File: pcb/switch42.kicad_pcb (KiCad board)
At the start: 2 copper layers, 114.3 x 81 mm, 83 parts, among them J1 MJ-4PP-9, SW1 SW_PUSH, SW10 SW_PUSH, SW11 SW_PUSH, SW12 SW_PUSH, SW13 SW_PUSH, SW14 SW_PUSH, SW15 SW_PUSH, SW16 SW_PUSH, SW17 SW_PUSH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

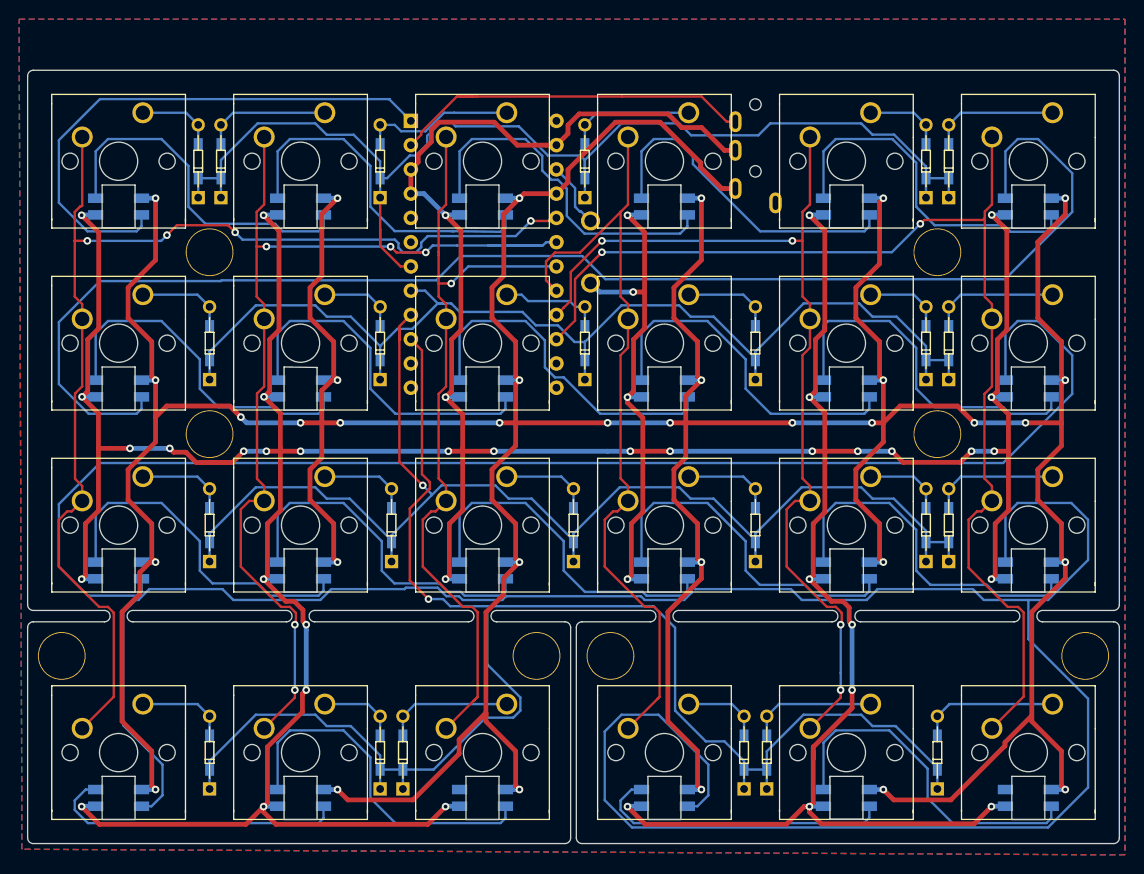
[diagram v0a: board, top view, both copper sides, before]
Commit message: Slightly modify footprint silks
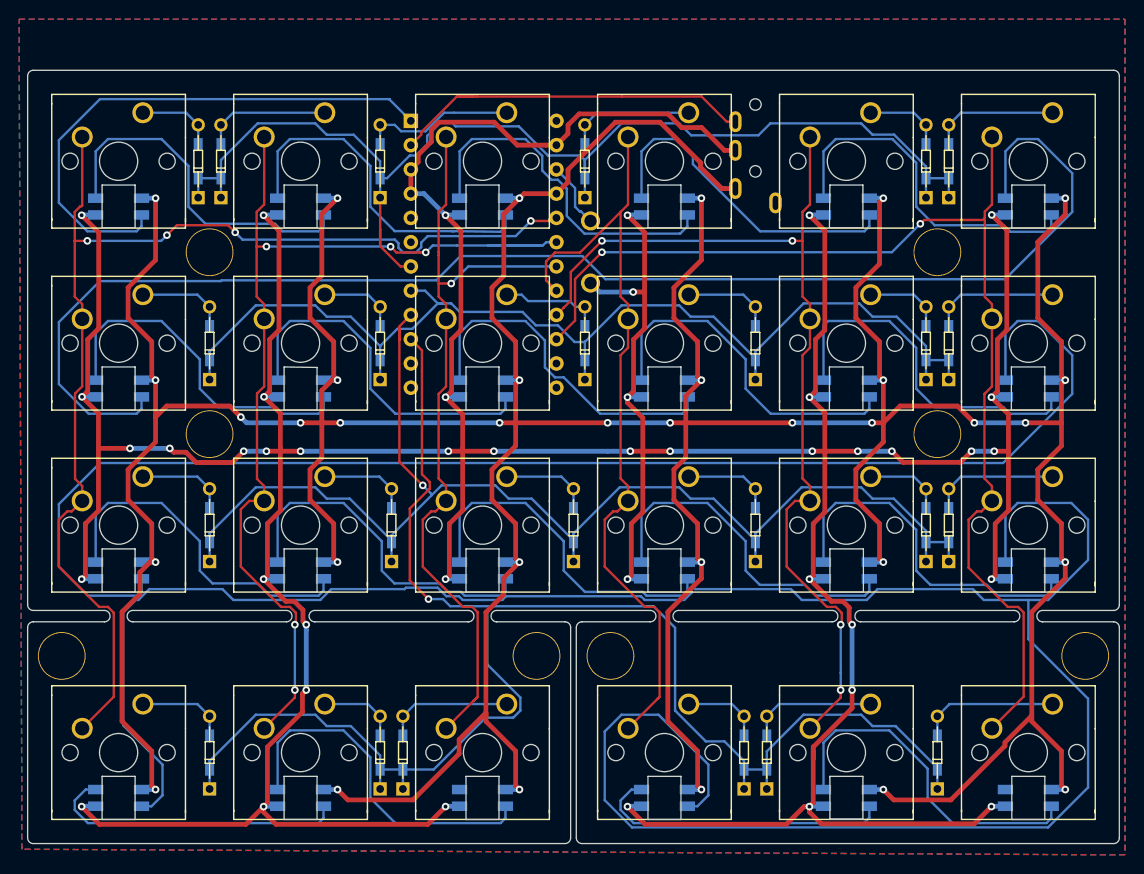
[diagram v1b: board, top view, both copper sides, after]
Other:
- board text added: "* switch42 v0.21 designed by @zk_phi *"
- board text removed: "* switch42 v0.2 designed by @zk_phi *"

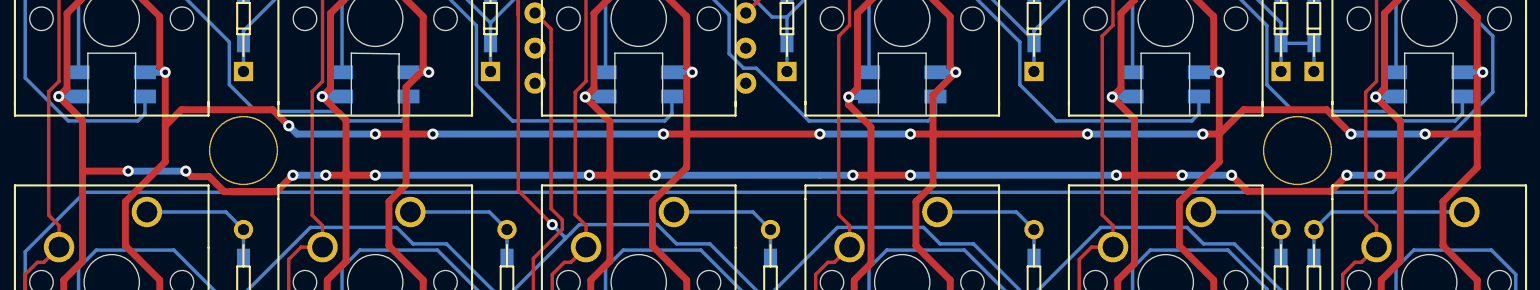
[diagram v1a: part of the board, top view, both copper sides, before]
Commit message: Refactoring: Reduce redundant vias
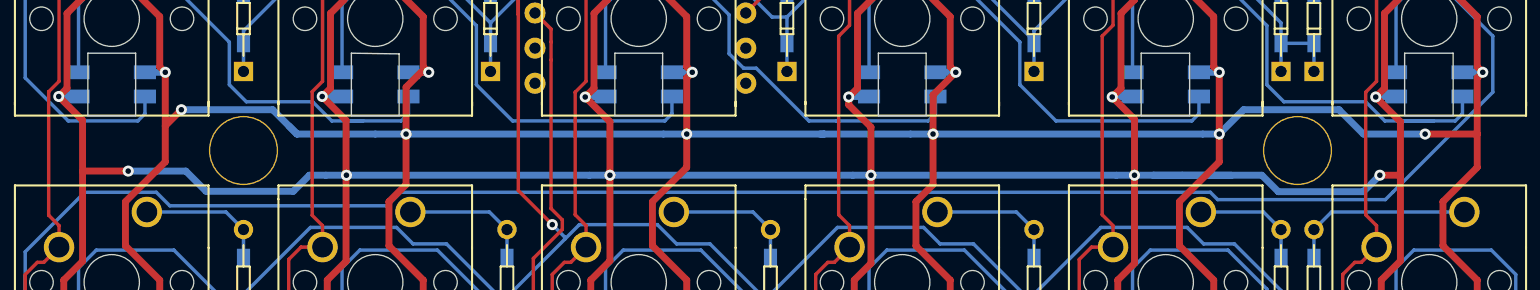
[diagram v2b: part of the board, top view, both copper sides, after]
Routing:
- net GND: track 576.0 -> 578.7 mm, vias 43 -> 35
- net Net-(L18-Pad1): track 37.8 -> 40.0 mm
- net VCC: track 568.5 -> 569.6 mm, vias 34 -> 30
- net Net-(L22-Pad1): track 146.8 -> 147.9 mm
- net Net-(L2-Pad1): track 36.6 -> 37.6 mm

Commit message: Add pads for LED strip and uniform the weight of silk text
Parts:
- added J2: Conn_01x03, kbd:StripLED_rev-irreversible, F.Cu at (74.2, 75.9)
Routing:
- net led: track 57.2 -> 103.5 mm, vias 0 -> 2
- net GND: track 578.7 -> 582.8 mm
- net VCC: track 569.6 -> 571.0 mm
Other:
- board text added: "GND"
- board text added: "LED"
- board text added: "Vcc"

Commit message: Change silk texts for the LED strip
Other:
- board text added: "+"
- board text added: "-"
- board text removed: "GND"
- board text removed: "LED"
- board text removed: "Vcc"
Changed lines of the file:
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@@
   (general
     (thickness 1.6)
-    (drawings 171)
+    (drawings 172)
     (tracks 1252)
     (zones 0)
@@
       (net 32 GND))
   )
-  (gr_text GND (at 76.830332 75.83109) (layer B.SilkS)
+  (gr_line (start 74.15141 77.021722) (end 75.6397 77.021722) (layer B.SilkS) (width 0.12))
+  (gr_line (start 74.15141 69.580272) (end 75.6397 69.580272) (layer B.SilkS) (width 0.12))
+  (gr_text - (at 75.6397 75.83109) (layer B.SilkS)
     (effects (font (size 1 1) (thickness 0.15)) (justify mirror))
   )
-  (gr_text LED (at 76.532674 73.449826) (layer B.SilkS)
+  (gr_text + (at 75.6397 70.770904) (layer B.SilkS)
     (effects (font (size 1 1) (thickness 0.15)) (justify mirror))
   )
-  (gr_text Vcc (at 76.532674 70.770904) (layer B.SilkS)
-    (effects (font (size 1 1) (thickness 0.15)) (justify mirror))
-  )

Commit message: Make diode line around thumb clusters safer
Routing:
- net row3: track 168.3 -> 175.1 mm, vias 1 -> 3
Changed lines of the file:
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@@
     (thickness 1.6)
     (drawings 172)
-    (tracks 1252)
+    (tracks 1255)
     (zones 0)
     (modules 84)
@@
   (segment (start 70.2818 107.978098) (end 70.2818 108.264528) (width 0.25) (layer B.Cu) (net 7) (status 30))
   (segment (start 75.121801 102.524527) (end 81.352797 102.524527) (width 0.25) (layer B.Cu) (net 7))
-  (via (at 93.201522 90.416332) (size 0.8) (drill 0.4) (layers F.Cu B.Cu) (net 7))
-  (segment (start 91.2368 88.45161) (end 93.201522 90.416332) (width 0.25) (layer F.Cu) (net 7))
-  (segment (start 91.2368 80.95242) (end 91.2368 88.45161) (width 0.25) (layer F.Cu) (net 7))
-  (segment (start 93.331207 78.162011) (end 93.331207 78.858013) (width 0.25) (layer F.Cu) (net 7))
-  (segment (start 92.517615 77.348419) (end 93.331207 78.162011) (width 0.25) (layer F.Cu) (net 7))
-  (segment (start 93.331207 78.858013) (end 91.2368 80.95242) (width 0.25) (layer F.Cu) (net 7))
-  (segment (start 95.472923 91.164001) (end 100.001248 91.164001) (width 0.25) (layer B.Cu) (net 7))
-  (segment (start 94.725254 90.416332) (end 95.472923 91.164001) (width 0.25) (layer B.Cu) (net 7))
-  (segment (start 93.201522 90.416332) (end 94.725254 90.416332) (width 0.25) (layer B.Cu) (net 7))
-  (segment (start 93.740802 108.264528) (end 90.522425 108.264528) (width 0.25) (layer B.Cu) (net 7) (status 20))
+  (via (at 92.308548 73.152168) (size 0.8) (drill 0.4) (layers F.Cu B.Cu) (net 7))
+  (segment (start 92.443133 73.017583) (end 92.308548 73.152168) (width 0.25) (layer F.Cu) (net 7))
+  (segment (start 92.443133 64.297235) (end 92.443133 73.017583) (width 0.25) (layer F.Cu) (net 7))
+  (segment (start 91.356132 63.210234) (end 92.443133 64.297235) (width 0.25) (layer F.Cu) (net 7))
+  (via (at 106.89379 74.045142) (size 0.8) (drill 0.4) (layers F.Cu B.Cu) (net 7))
+  (segment (start 93.201522 74.045142) (end 106.89379 74.045142) (width 0.25) (layer B.Cu) (net 7))
+  (segment (start 92.308548 73.152168) (end 93.201522 74.045142) (width 0.25) (layer B.Cu) (net 7))
+  (via (at 106.89379 90.956964) (size 0.8) (drill 0.4) (layers F.Cu B.Cu) (net 7))
+  (segment (start 106.89379 74.045142) (end 106.89379 90.956964) (width 0.25) (layer F.Cu) (net 7))
+  (segment (start 126.241175 107.364528) (end 126.241175 108.264528) (width 0.25) (layer B.Cu) (net 7))
+  (segment (start 124.191174 105.314527) (end 126.241175 107.364528) (width 0.25) (layer B.Cu) (net 7))
+  (segment (start 122.242797 105.314527) (end 124.191174 105.314527) (width 0.25) (layer B.Cu) (net 7))
+  (segment (start 119.021799 102.093529) (end 122.242797 105.314527) (width 0.25) (layer B.Cu) (net 7))
   (segment (start 99.170801 102.834529) (end 93.740802 108.264528) (width 0.25) (layer B.Cu) (net 7))
-  (segment (start 102.821801 102.093529) (end 102.080801 102.834529) (width 0.25) (layer B.Cu) (net 7))
+  (segment (start 93.740802 108.264528) (end 90.522425 108.264528) (width 0.25) (layer B.Cu) (net 7))
+  (segment (start 102.080801 102.834529) (end 99.170801 102.834529) (width 0.25) (layer B.Cu) (net 7))
   (segment (start 102.821801 100.725527) (end 102.821801 102.093529) (width 0.25) (layer B.Cu) (net 7))
   (segment (start 99.347564 97.25129) (end 102.821801 100.725527) (width 0.25) (layer B.Cu) (net 7))
+  (segment (start 102.821801 102.093529) (end 102.080801 102.834529) (width 0.25) (layer B.Cu) (net 7))
   (segment (start 99.347564 91.817685) (end 99.347564 97.25129) (width 0.25) (layer B.Cu) (net 7))
-  (segment (start 102.080801 102.834529) (end 99.170801 102.834529) (width 0.25) (layer B.Cu) (net 7))
-  (segment (start 100.001248 91.164001) (end 99.347564 91.817685) (width 0.25) (layer B.Cu) (net 7))
-  (segment (start 126.241175 107.364528) (end 126.241175 108.264528) (width 0.25) (layer B.Cu) (net 7) (status 20))
-  (segment (start 124.191174 105.314527) (end 126.241175 107.364528) (width 0.25) (layer B.Cu) (net 7))
-  (segment (start 122.242797 105.314527) (end 124.191174 105.314527) (width 0.25) (layer B.Cu) (net 7))
-  (segment (start 100.001248 91.164001) (end 116.762912 91.164001) (width 0.25) (layer B.Cu) (net 7))
-  (segment (start 119.021799 102.093529) (end 122.242797 105.314527) (width 0.25) (layer B.Cu) (net 7))
-  (segment (start 119.021799 93.422888) (end 119.021799 102.093529) (width 0.25) (layer B.Cu) (net 7))
-  (segment (start 116.762912 91.164001) (end 119.021799 93.422888) (width 0.25) (layer B.Cu) (net 7))
-  (segment (start 92.517615 65.302955) (end 92.517615 66.603692) (width 0.25) (layer F.Cu) (net 7))
-  (segment (start 91.356132 63.210234) (end 92.517615 64.371717) (width 0.25) (layer F.Cu) (net 7))
-  (segment (start 92.517615 66.603692) (end 92.517615 77.348419) (width 0.25) (layer F.Cu) (net 7))
-  (segment (start 92.517615 64.371717) (end 92.517615 65.302955) (width 0.25) (layer F.Cu) (net 7))
+  (segment (start 99.933295 91.231954) (end 99.347564 91.817685) (width 0.25) (layer B.Cu) (net 7))
+  (segment (start 106.053115 91.231954) (end 99.933295 91.231954) (width 0.25) (layer B.Cu) (net 7))
+  (segment (start 106.328105 90.956964) (end 106.053115 91.231954) (width 0.25) (layer B.Cu) (net 7))
+  (segment (start 106.89379 90.956964) (end 106.328105 90.956964) (width 0.25) (layer B.Cu) (net 7))
+  (segment (start 116.79208 91.231954) (end 119.021799 93.461673) (width 0.25) (layer B.Cu) (net 7))
+  (segment (start 107.734465 91.231954) (end 116.79208 91.231954) (width 0.25) (layer B.Cu) (net 7))
+  (segment (start 107.459475 90.956964) (end 107.734465 91.231954) (width 0.25) (layer B.Cu) (net 7))
+  (segment (start 119.021799 93.461673) (end 119.021799 94.583544) (width 0.25) (layer B.Cu) (net 7))
+  (segment (start 106.89379 90.956964) (end 107.459475 90.956964) (width 0.25) (layer B.Cu) (net 7))
+  (segment (start 119.021799 94.583544) (end 119.021799 102.093529) (width 0.25) (layer B.Cu) (net 7))
+  (segment (start 119.021799 93.422888) (end 119.021799 94.583544) (width 0.25) (layer B.Cu) (net 7))
   (segment (start 70.2818 102.679528) (end 70.2818 104.714528) (width 0.25) (layer B.Cu) (net 8) (status 30))
   (segment (start 69.0118 101.409528) (end 70.2818 102.679528) (width 0.25) (layer B.Cu) (net 8) (status 20))
@@
   (segment (start 114.0968 80.137) (end 112.996801 81.236999) (width 0.25) (layer F.Cu) (net 38) (status 10))
   (segment (start 112.996801 81.236999) (end 112.527799 81.236999) (width 0.25) (layer F.Cu) (net 38))
-  (segment (start 116.830865 91.231954) (end 117.416596 91.817685) (width 0.25) (layer F.Cu) (net 38))
   (segment (start 115.863808 91.231954) (end 116.830865 91.231954) (width 0.25) (layer F.Cu) (net 38))
   (segment (start 111.651799 87.019945) (end 115.863808 91.231954) (width 0.25) (layer F.Cu) (net 38))
@@
   (segment (start 106.596132 58.130234) (end 105.509131 57.043233) (width 0.25) (layer F.Cu) (net 38))
   (segment (start 113.312581 49.884501) (end 111.47629 51.720792) (width 0.25) (layer F.Cu) (net 38))
+  (segment (start 116.830865 91.231954) (end 117.416596 91.817685) (width 0.25) (layer F.Cu) (net 38))
   (segment (start 133.1468 59.531366) (end 133.1468 61.087) (width 0.25) (layer F.Cu) (net 39) (status 20))
   (segment (start 132.362693 58.747259) (end 133.1468 59.531366) (width 0.25) (layer F.Cu) (net 39))

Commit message: Change version name
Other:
- board text added: "* switch42 v0.3 designed by @zk_phi *"
- board text removed: "* switch42 v0.21 designed by @zk_phi *"
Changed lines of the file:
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@@
     (effects (font (size 5 5) (thickness 0.15)) (justify mirror))
   )
-  (gr_text "* switch42 v0.21 designed by @zk_phi *" (at 136.957248 95.17886) (layer F.Mask)
+  (gr_text "* switch42 v0.3 designed by @zk_phi *" (at 136.957248 95.17886) (layer F.Mask)
     (effects (font (size 1.2 1.2) (thickness 0.3)))
   )
-  (gr_text "* switch42 v0.21 designed by @zk_phi *" (at 79.806912 95.17886) (layer F.Mask)
+  (gr_text "* switch42 v0.3 designed by @zk_phi *" (at 79.806912 95.17886) (layer F.Mask)
     (effects (font (size 1.2 1.2) (thickness 0.3)))
   )

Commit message: Use components from my own library
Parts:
- D1, D10, D11, D12, D13, D14, D15, D16, D17, D18, D19, D2, D20, D21, D22, D23, D24, D3, D4, D5, D6, D7, D8, D9: footprint kbd:D3_TH_SMD_irreversible -> phi-kbd-library:D_TH_SMD-irreversible
- J1: footprint SMKJP:CON_MJ-4PP-9-kbd -> phi-kbd-library:MJ-4PP-9-irreversible
- J2: footprint kbd:StripLED_rev-irreversible -> phi-kbd-library:StripLED-irreversible; moved to B.Cu
- L1, L10, L11, L12, L13, L14, L15, L16, L17, L18, L19, L2, L20, L21, L22, L23, L24, L3, L4, L5, L6, L7, L8, L9: footprint kbd:SK6812MINI_rev_irreversible -> phi-kbd-library:SK6812MINI-irreversible; moved to B.Cu
- SW1: footprint kbd:ResetSW-irreversible -> phi-kbd-library:ResetSW-irreversible; moved to B.Cu
- SW10, SW11, SW12, SW13, SW14, SW15, SW16, SW17, SW18, SW19, SW2, SW20, SW21, SW22, SW23, SW24, SW25, SW3, SW4, SW5, SW6, SW7, SW8, SW9: footprint SMKJP:SW_Cherry_MX1A_1.00u_PCB_nosilk -> phi-kbd-library:MX_1.00u-irreversible
- U1: footprint SMKJP:BOARD_Pro_Micro_Reversed-conthrough -> phi-kbd-library:ProMicro_Reversed_Conthrough-irreversible
- moved J2 5.08 mm to (74.2, 70.8)
- turned SW1 to 270 degrees

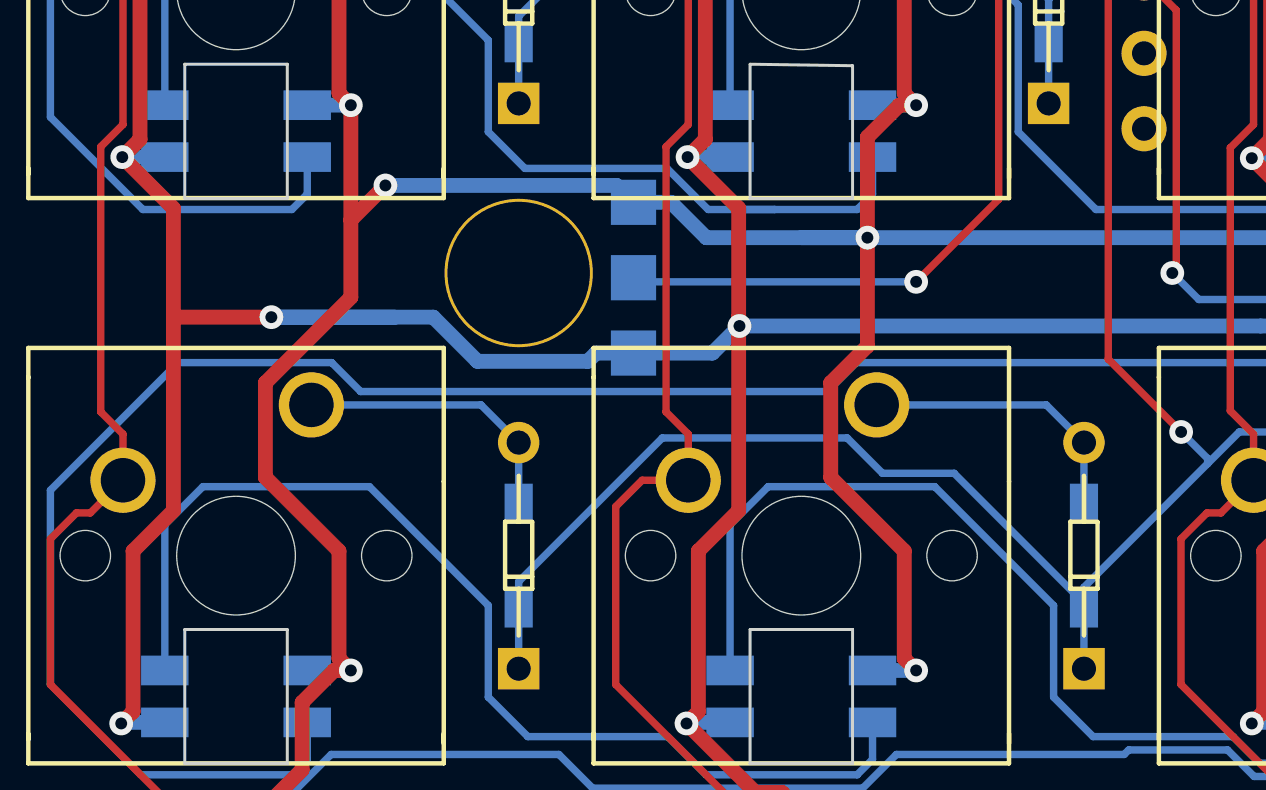
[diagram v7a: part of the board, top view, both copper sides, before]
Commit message: Update LED strip footprint and adjust position, silk
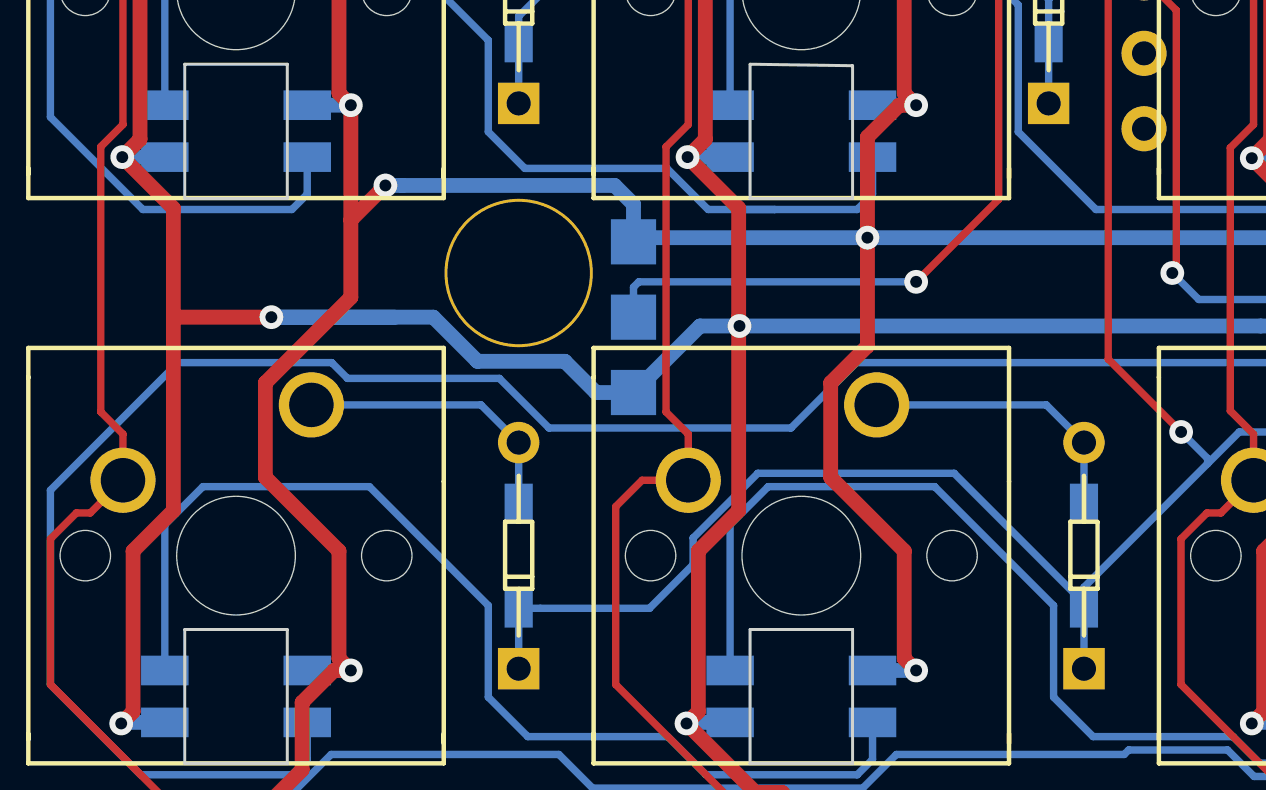
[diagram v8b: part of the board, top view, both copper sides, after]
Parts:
- J2: footprint phi-kbd-library:StripLED-irreversible -> phi-kbd-library:StripLED-1mm-irreversible
- moved J2 1.33 mm to (74.2, 72.1)
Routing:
- net VCC: track 571.0 -> 569.6 mm
- net led: track 103.5 -> 104.5 mm
- net Net-(L22-Pad1): track 147.9 -> 148.9 mm
- net row2: track 133.8 -> 132.8 mm
- net GND: track 582.8 -> 583.7 mm
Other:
- board text added: "DIN"
- board text added: "GND"
- board text added: "VCC"
- board text removed: "+"
- board text removed: "-"
